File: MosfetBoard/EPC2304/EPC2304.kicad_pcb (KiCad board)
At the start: 4 copper layers, 120 x 75 mm, 170 parts, among them J10 DriverConn, J14 BATT-Conn2, J4 PhaseConn, J5 PhaseConn, J6 PhaseConn, J7 DriverConn, J8 DriverConn, J9 BATT-Conn1, Q1 EPC2304, Q13 EPC2304, Q14 EPC2304, Q15 EPC2304, Q2 EPC2304, Q3 EPC2304, Q4 EPC2304, Q5 EPC2304, Q6 EPC2304, Q7 EPC2304, Q8 EPC2304, Q9 EPC2304, U1 2EDF7275KXUMA1, U2 2EDF7275KXUMA1, U3 2EDF7275KXUMA1, U4 MT9223CT-50BR5, U5 MT9223CT-50BR5, U6 MT9223CT-50BR5

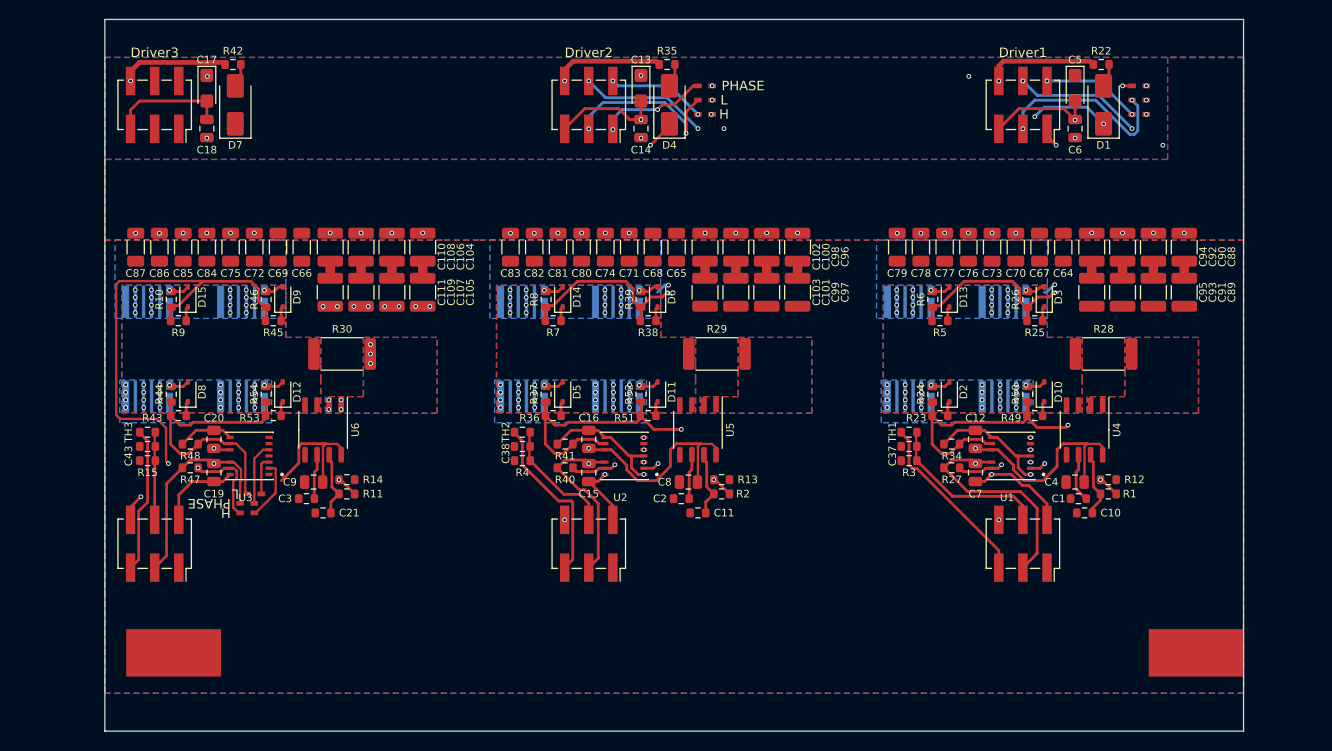
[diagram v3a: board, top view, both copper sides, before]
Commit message: v2.8.0 - Small Hall sensors
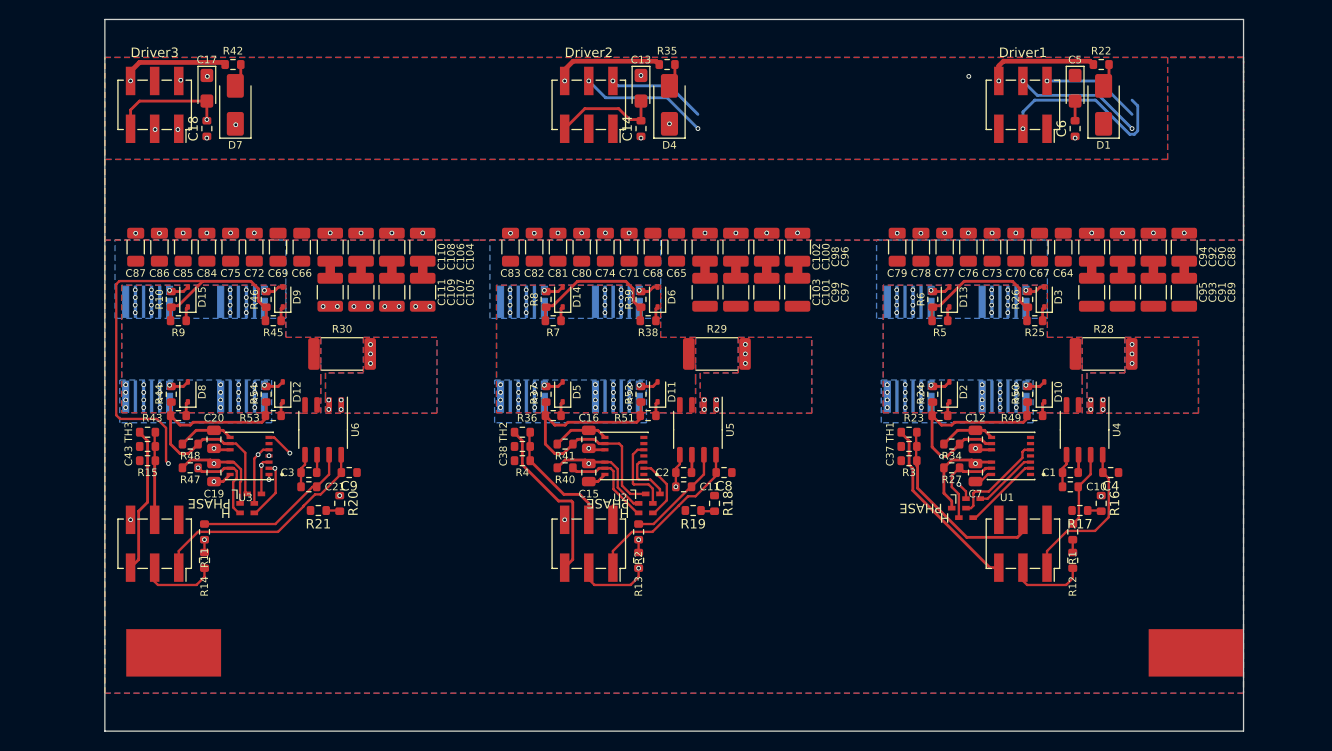
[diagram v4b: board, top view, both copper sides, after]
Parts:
- added R16: 150k, Resistor_SMD:R_0603_1608Metric, F.Cu at (210.0, 105.0)
- added R17: 2.7k, Resistor_SMD:R_0603_1608Metric, F.Cu at (207.8, 105.8)
- added R18: 150k, Resistor_SMD:R_0603_1608Metric, F.Cu at (169.2, 105.0)
- added R19: 2.7k, Resistor_SMD:R_0603_1608Metric, F.Cu at (167.0, 105.8)
- added R20: 150k, Resistor_SMD:R_0603_1608Metric, F.Cu at (129.8, 105.0)
- added R21: 2.7k, Resistor_SMD:R_0603_1608Metric, F.Cu at (127.5, 105.8)
- C14, C18, C4, C6, C8, C9: footprint Capacitor_SMD:C_0805_2012Metric -> GigaVescLibs:C_0603_1608Metric_L
- moved JP1 48.4 mm to (195.0, 105.5), turned to 180 degrees
- moved JP3 46.3 mm to (195.8, 106.5), turned to 180 degrees
- moved JP2 45.5 mm to (196.5, 104.5), turned to 180 degrees
- moved JP5 44.4 mm to (162.0, 105.0), turned to 180 degrees
- moved JP7 42.5 mm to (162.0, 106.0), turned to 180 degrees
- moved JP6 41.9 mm to (162.8, 104.0), turned to 180 degrees
- moved R14 17.2 mm to (115.5, 111.0), turned to 90 degrees
- moved R11 15.5 mm to (115.5, 108.0), turned to 90 degrees
- moved R13 12.2 mm to (161.2, 111.0), turned to 90 degrees
- moved R2 9.62 mm to (161.2, 108.0), turned to 90 degrees
- moved R12 9.29 mm to (207.0, 111.0), turned to 90 degrees
- moved R1 5.48 mm to (207.0, 108.0), turned to 90 degrees
- moved C4 3.88 mm to (211.0, 101.8), turned to 180 degrees
- moved C8 3.88 mm to (170.2, 101.8), turned to 180 degrees
- moved C9 3.88 mm to (130.8, 101.8), turned to 180 degrees
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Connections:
- net Net-(R28-Pad2) renamed /PhaseMosfets1/PHASE_OUT
- net Net-(R29-Pad2) renamed /PhaseMosfets2/PHASE_OUT
- net Net-(R30-Pad2) renamed /PhaseMosfets3/PHASE_OUT
- C1 pad 2: GNDA -> /PhaseMosfets1/SH-
- C10 pad 2: GNDA -> /PhaseMosfets1/SH-
- C11 pad 2: GNDA -> /PhaseMosfets2/SH-
- C15 pad 1: /PhaseMosfets2/FLOAT_VDD -> Net-(D4-K)
- C19 pad 1: /PhaseMosfets3/FLOAT_VDD -> Net-(D7-K)
- C2 pad 2: GNDA -> /PhaseMosfets2/SH-
- C21 pad 2: GNDA -> /PhaseMosfets3/SH-
- C3 pad 2: GNDA -> /PhaseMosfets3/SH-
- C4 pad 2: /PhaseMosfets1/DRV_POWER -> /PhaseMosfets1/5V_IN
- C7 pad 1: /PhaseMosfets1/FLOAT_VDD -> Net-(D1-K)
- C8 pad 2: /PhaseMosfets2/DRV_POWER -> /PhaseMosfets2/5V_IN
- C9 pad 2: /PhaseMosfets3/DRV_POWER -> /PhaseMosfets3/5V_IN
- D1 pad 1: /PhaseMosfets1/FLOAT_VDD -> Net-(D1-K)
- D4 pad 1: /PhaseMosfets2/FLOAT_VDD -> Net-(D4-K)
- D7 pad 1: /PhaseMosfets3/FLOAT_VDD -> Net-(D7-K)
- J4 pad 1: -BATT -> /PhaseMosfets1/5V_IN
- J4 pad 2: /PhaseMosfets1/FLOAT_VDD -> /PhaseMosfets1/V_SENSE
- J4 pad 3: GNDA -> /PhaseMosfets1/SH-
- J5 pad 1: -BATT -> /PhaseMosfets2/5V_IN
- J5 pad 2: /PhaseMosfets2/FLOAT_VDD -> /PhaseMosfets2/V_SENSE
- J5 pad 3: GNDA -> /PhaseMosfets2/SH-
- J6 pad 1: -BATT -> /PhaseMosfets3/5V_IN
- J6 pad 2: /PhaseMosfets3/FLOAT_VDD -> /PhaseMosfets3/V_SENSE
- J6 pad 3: GNDA -> /PhaseMosfets3/SH-
- R12 pad 1: GNDA -> /PhaseMosfets1/SH-
- R13 pad 1: GNDA -> /PhaseMosfets2/SH-
- R14 pad 1: GNDA -> /PhaseMosfets3/SH-
- U1 pad 13: /PhaseMosfets1/FLOAT_VDD -> Net-(D1-K)
- U2 pad 13: /PhaseMosfets2/FLOAT_VDD -> Net-(D4-K)
- U3 pad 13: /PhaseMosfets3/FLOAT_VDD -> Net-(D7-K)
- U4 pad 5: GNDA -> /PhaseMosfets1/SH-
- U4 pad 8: /PhaseMosfets1/DRV_POWER -> /PhaseMosfets1/5V_IN
- U5 pad 5: GNDA -> /PhaseMosfets2/SH-
- U5 pad 8: /PhaseMosfets2/DRV_POWER -> /PhaseMosfets2/5V_IN
- U6 pad 5: GNDA -> /PhaseMosfets3/SH-
- U6 pad 8: /PhaseMosfets3/DRV_POWER -> /PhaseMosfets3/5V_IN
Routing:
- net -BATT: track 143.0 -> 45.5 mm, vias 22 -> 20
- net Net-(D7-K): track 0.00 -> 81.6 mm, vias 0 -> 2
- net /PhaseMosfets3/H: track 6.38 -> 86.4 mm, vias 0 -> 2
- net /PhaseMosfets3/L: track 4.05 -> 82.2 mm, vias 0 -> 2
- net /PhaseMosfets3/LOCKOUT: track 6.66 -> 81.3 mm, vias 0 -> 2
- net /PhaseMosfets3/3.3V_IN: track 12.4 -> 86.1 mm, vias 0 -> 2
- net /PhaseMosfets1/FLOAT_VDD: track 59.1 -> 0.00 mm, vias 3 -> 0
- net /PhaseMosfets2/L: track 55.1 -> 5.63 mm, vias 3 -> 0
- net /PhaseMosfets1/PH: track 73.2 -> 25.3 mm, vias 3 -> 0
- net /PhaseMosfets2/FLOAT_VDD: track 47.0 -> 0.00 mm, vias 2 -> 0
- net /PhaseMosfets1/3.3V_IN: track 47.8 -> 1.95 mm, vias 2 -> 0
- net /PhaseMosfets2/PH: track 68.7 -> 26.0 mm, vias 3 -> 0
- net /PhaseMosfets1/PHASE: track 57.6 -> 16.4 mm, vias 43 -> 41
- net /PhaseMosfets2/LOCKOUT: track 48.4 -> 8.28 mm, vias 3 -> 0
- net /PhaseMosfets1/LOCKOUT: track 48.4 -> 10.5 mm, vias 3 -> 0
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
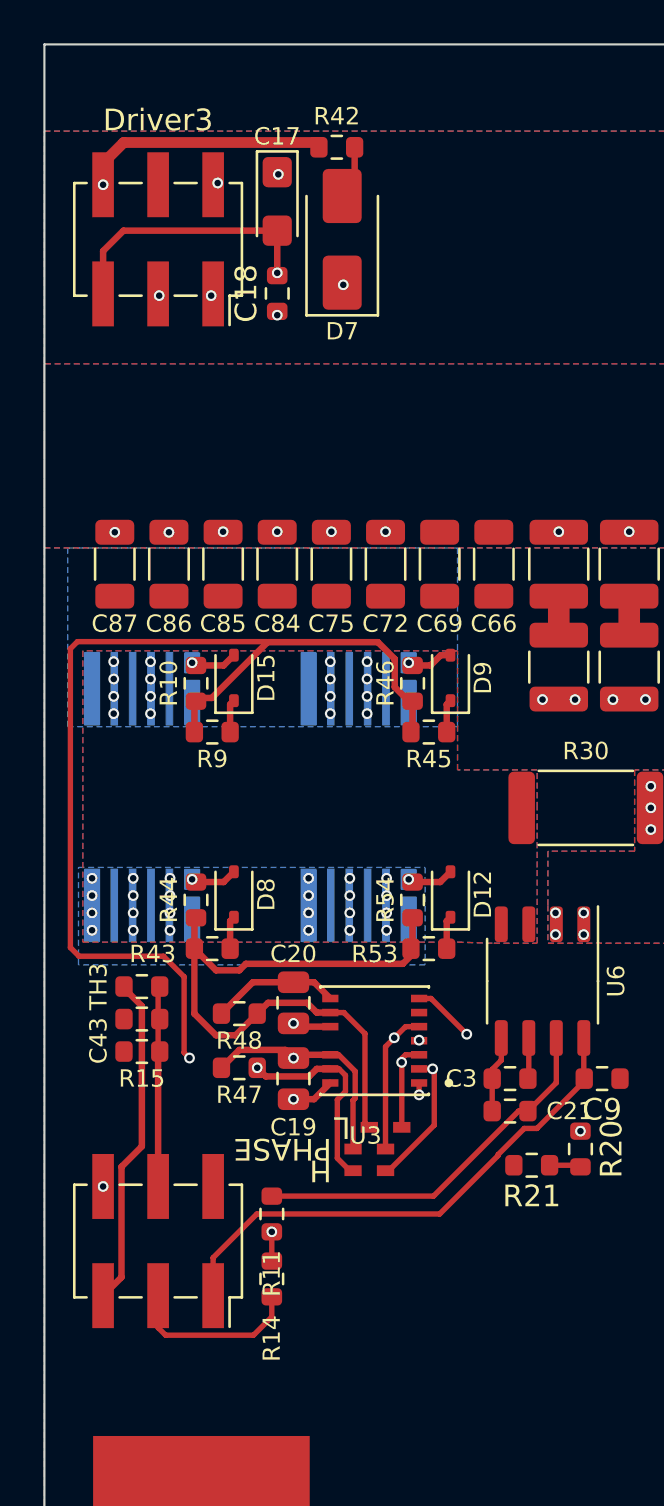
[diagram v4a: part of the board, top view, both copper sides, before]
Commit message: v2.10.0 - Low side shunt and hall sensor - logic routed
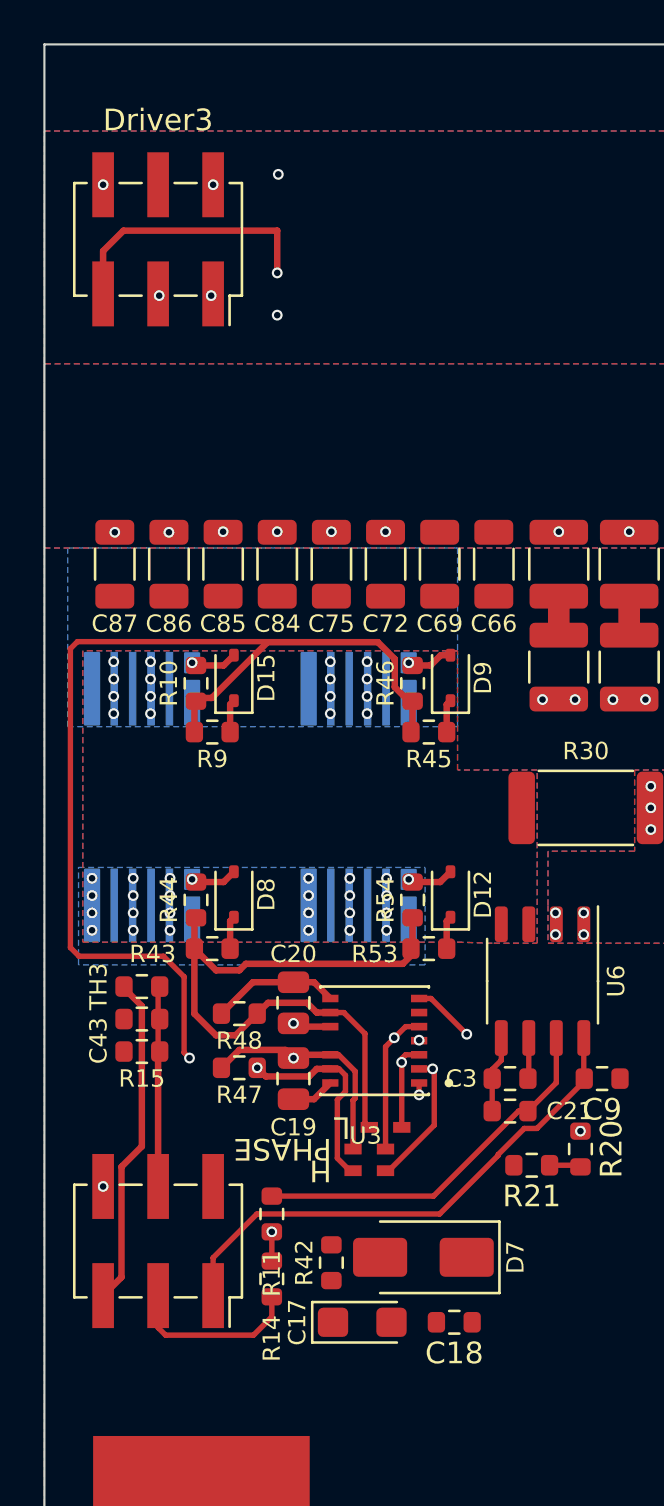
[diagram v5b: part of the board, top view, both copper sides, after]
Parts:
- moved C17 51.9 mm to (119.7, 113.0), turned to 0 degrees
- moved R42 51.5 mm to (118.2, 110.2), turned to -90 degrees
- moved C18 48.2 mm to (123.9, 113.0), turned to 180 degrees
- moved D7 47.1 mm to (122.5, 110.0), turned to 180 degrees
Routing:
- net Net-(D7-K): track 81.6 -> 2.01 mm, vias 2 -> 0
- net /PhaseMosfets3/DRV_POWER: track 61.1 -> 50.6 mm
- net Net-(D7-A): track 2.49 -> 0.00 mm

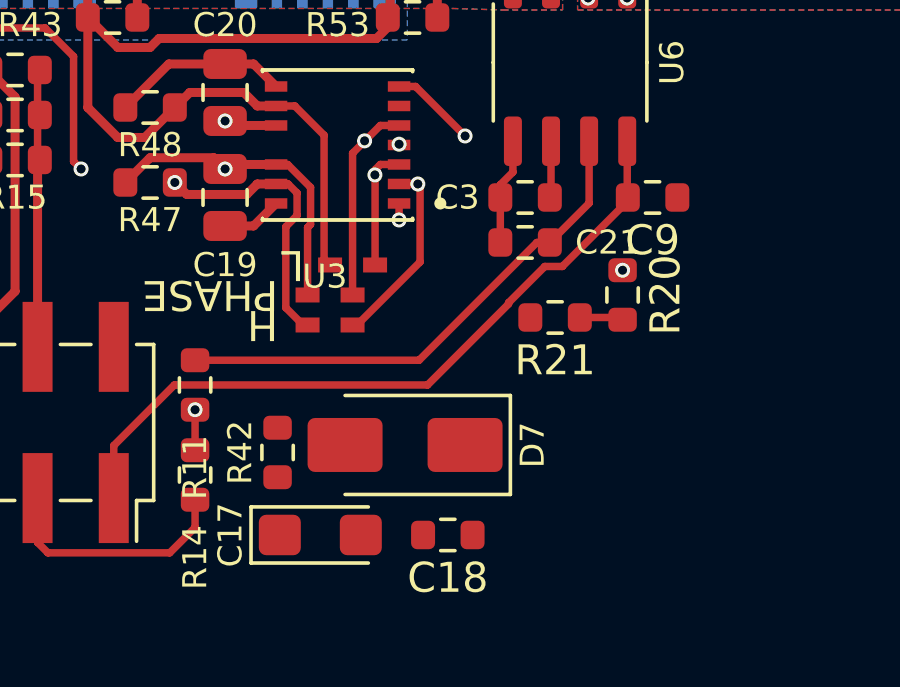
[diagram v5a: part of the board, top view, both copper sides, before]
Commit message: v2.10.0 - Low side shunt and hall sensor - current filters
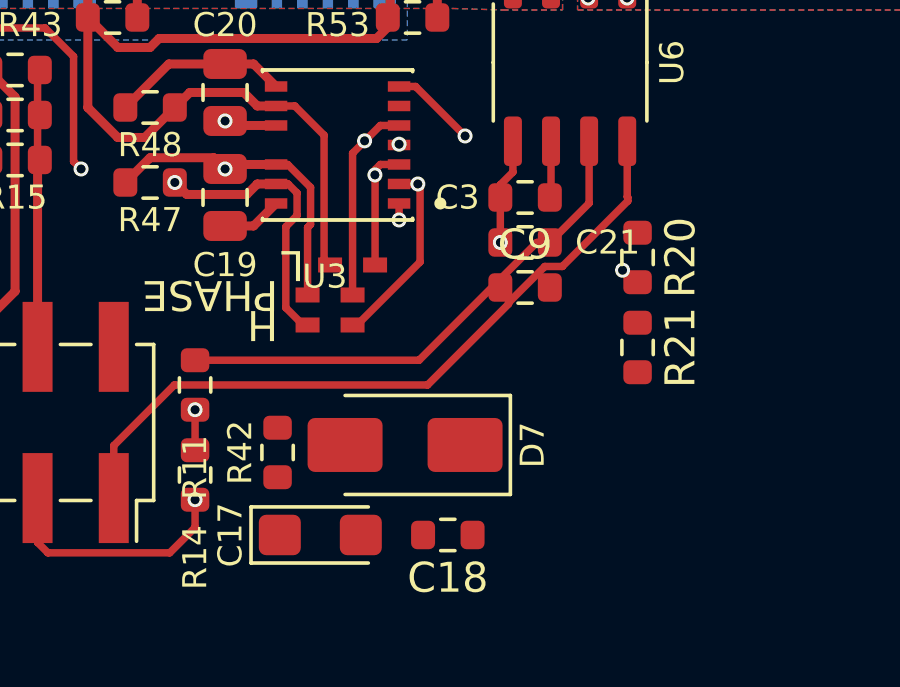
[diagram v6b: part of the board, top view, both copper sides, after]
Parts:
- moved C9 5.20 mm to (126.5, 104.8), turned to 0 degrees
- moved R21 2.93 mm to (130.2, 106.8), turned to -90 degrees
- moved R20 1.35 mm to (130.2, 103.8)
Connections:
- C4 pad 1: -BATT -> /PhaseMosfets1/SH-
- C8 pad 1: -BATT -> /PhaseMosfets2/SH-
- C9 pad 1: -BATT -> /PhaseMosfets3/SH-
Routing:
- net /PhaseMosfets3/SH-: track 11.7 -> 25.4 mm, vias 0 -> 2
- net /PhaseMosfets3/V_SENSE: track 1.46 -> 0.00 mm, vias 0 -> 1
- net /PhaseMosfets3/PHASE_OUT: vias 8 -> 7
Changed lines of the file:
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@@
       (stroke (width 0.1) (type solid)) (layer "F.Fab"))
     (pad "1" smd roundrect (at -0.825 0 180) (size 0.8 0.95) (layers "F.Cu" "F.Paste" "F.Mask") (roundrect_rratio 0.25)
-      (net 3 "-BATT") (pintype "passive"))
+      (net 11 "/PhaseMosfets1/SH-") (pintype "passive"))
     (pad "2" smd roundrect (at 0.825 0 180) (size 0.8 0.95) (layers "F.Cu" "F.Paste" "F.Mask") (roundrect_rratio 0.25)
       (net 78 "/PhaseMosfets1/5V_IN") (pintype "passive"))
@@
   )
   (footprint "Resistor_SMD:R_0603_1608Metric" (layer "F.Cu")
-    (at 127.5 105.75 180)
+    (at 130.25 106.75 -90)
     (descr "Resistor SMD 0603 (1608 Metric), square (rectangular) end terminal, IPC_7351 nominal, (Body size source: IPC-SM-782 page 72, https://www.pcb-3d.com/wordpress/wp-content/uploads/ipc-sm-782a_amendment_1_and_2.pdf), generated with kicad-footprint-generator")
     (tags "resistor")
@@
     (property "ki_keywords" "R res resistor")
     (attr smd)
-    (fp_text reference "R21" (at 0 -1.43) (layer "F.SilkS")
+    (fp_text reference "R21" (at 0 -1.43 -270) (layer "F.SilkS")
         (effects (font (size 1 1) (thickness 0.15)))
     )
-    (fp_text value "2.7k" (at 0 1.43) (layer "F.Fab")
+    (fp_text value "2.7k" (at 0 1.43 -270) (layer "F.Fab")
         (effects (font (size 1 1) (thickness 0.15)))
     )
-    (fp_text user "${REFERENCE}" (at 0 0) (layer "F.Fab")
+    (fp_text user "${REFERENCE}" (at 0 0 -270) (layer "F.Fab")
         (effects (font (size 0.4 0.4) (thickness 0.06)))
     )
@@
     (fp_line (start 0.8 0.4125) (end -0.8 0.4125)
       (stroke (width 0.1) (type solid)) (layer "F.Fab"))
-    (pad "1" smd roundrect (at -0.825 0 180) (size 0.8 0.95) (layers "F.Cu" "F.Paste" "F.Mask") (roundrect_rratio 0.25)
+    (pad "1" smd roundrect (at -0.825 0 270) (size 0.8 0.95) (layers "F.Cu" "F.Paste" "F.Mask") (roundrect_rratio 0.25)
       (net 95 "/PhaseMosfets3/V_SENSE") (pintype "passive"))
-    (pad "2" smd roundrect (at 0.825 0 180) (size 0.8 0.95) (layers "F.Cu" "F.Paste" "F.Mask") (roundrect_rratio 0.25)
+    (pad "2" smd roundrect (at 0.825 0 270) (size 0.8 0.95) (layers "F.Cu" "F.Paste" "F.Mask") (roundrect_rratio 0.25)
       (net 3 "-BATT") (pintype "passive"))
     (model "${KICAD6_3DMODEL_DIR}/Resistor_SMD.3dshapes/R_0603_1608Metric.wrl"
@@
       (stroke (width 0.1) (type solid)) (layer "F.Fab"))
     (pad "1" smd roundrect (at -0.825 0 180) (size 0.8 0.95) (layers "F.Cu" "F.Paste" "F.Mask") (roundrect_rratio 0.25)
-      (net 3 "-BATT") (pintype "passive"))
+      (net 17 "/PhaseMosfets2/SH-") (pintype "passive"))
     (pad "2" smd roundrect (at 0.825 0 180) (size 0.8 0.95) (layers "F.Cu" "F.Paste" "F.Mask") (roundrect_rratio 0.25)
       (net 80 "/PhaseMosfets2/5V_IN") (pintype "passive"))
@@
   )
   (footprint "Resistor_SMD:R_0603_1608Metric" (layer "F.Cu")
-    (at 129.75 105 -90)
+    (at 130.25 103.75 -90)
     (descr "Resistor SMD 0603 (1608 Metric), square (rectangular) end terminal, IPC_7351 nominal, (Body size source: IPC-SM-782 page 72, https://www.pcb-3d.com/wordpress/wp-content/uploads/ipc-sm-782a_amendment_1_and_2.pdf), generated with kicad-footprint-generator")
     (tags "resistor")
@@
   )
   (footprint "GigaVescLibs:C_0603_1608Metric_L" (layer "F.Cu")
-    (at 130.75 101.75 180)
+    (at 126.5 104.75)
     (descr "Resistor SMD 0603 (1608 Metric), square (rectangular) end terminal, IPC_7351 nominal, (Body size source: IPC-SM-782 page 72, https://www.pcb-3d.com/wordpress/wp-content/uploads/ipc-sm-782a_amendment_1_and_2.pdf), generated with kicad-footprint-generator")
     (tags "resistor")
@@
     (fp_line (start 0.8 0.4125) (end -0.8 0.4125)
       (stroke (width 0.1) (type solid)) (layer "F.Fab"))
-    (pad "1" smd roundrect (at -0.825 0 180) (size 0.8 0.95) (layers "F.Cu" "F.Paste" "F.Mask") (roundrect_rratio 0.25)
-      (net 3 "-BATT") (pintype "passive"))
-    (pad "2" smd roundrect (at 0.825 0 180) (size 0.8 0.95) (layers "F.Cu" "F.Paste" "F.Mask") (roundrect_rratio 0.25)
+    (pad "1" smd roundrect (at -0.825 0) (size 0.8 0.95) (layers "F.Cu" "F.Paste" "F.Mask") (roundrect_rratio 0.25)
+      (net 23 "/PhaseMosfets3/SH-") (pintype "passive"))
+    (pad "2" smd roundrect (at 0.825 0) (size 0.8 0.95) (layers "F.Cu" "F.Paste" "F.Mask") (roundrect_rratio 0.25)
       (net 90 "/PhaseMosfets3/5V_IN") (pintype "passive"))
     (model "${KICAD7_3DMODEL_DIR}/Capacitor_SMD.3dshapes/C_0603_1608Metric.wrl"
@@
   (segment (start 125.675 101.325) (end 125.675 101.75) (width 0.25) (layer "F.Cu") (net 23))
   (segment (start 115.5 112.75) (end 114.655 113.595) (width 0.25) (layer "F.Cu") (net 23))
+  (via (at 115.5 111.825) (size 0.5) (drill 0.3) (layers "F.Cu" "B.Cu") (net 23))
+  (via (at 125.675 103.25) (size 0.5) (drill 0.3) (layers "F.Cu" "B.Cu") (net 23))
+  (segment (start 124.075 103.25) (end 125.675 103.25) (width 0.25) (layer "In2.Cu") (net 23))
+  (segment (start 115.5 111.825) (end 124.075 103.25) (width 0.25) (layer "In2.Cu") (net 23))
   (segment (start 210.825 60.425) (end 210.25 61) (width 0.3) (layer "F.Cu") (net 24))
   (segment (start 210.825 58.75) (end 210.825 60.425) (width 0.3) (layer "F.Cu") (net 24))
@@
   (segment (start 167.9 105.825) (end 167.825 105.75) (width 0.25) (layer "F.Cu") (net 94))
   (segment (start 169.25 105.825) (end 167.9 105.825) (width 0.25) (layer "F.Cu") (net 94))
-  (segment (start 129.675 105.75) (end 129.75 105.825) (width 0.25) (layer "F.Cu") (net 95))
-  (segment (start 128.325 105.75) (end 129.675 105.75) (width 0.25) (layer "F.Cu") (net 95))
+  (via (at 129.75 104.175) (size 0.5) (drill 0.3) (layers "F.Cu" "B.Cu") (net 95))
   (segment (start 210 104.175) (end 210 104.25) (width 0.25) (layer "F.Cu") (net 96))
   (via (at 210.2 95.1) (size 0.5) (drill 0.3) (layers "F.Cu" "B.Cu") (net 96))
@@
   (via (at 129.9 95.1) (size 0.5) (drill 0.3) (layers "F.Cu" "B.Cu") (net 98))
   (via (at 128.6 95.1) (size 0.5) (drill 0.3) (layers "F.Cu" "B.Cu") (net 98))
-  (via (at 129.75 104.175) (size 0.5) (drill 0.3) (layers "F.Cu" "B.Cu") (net 98))
   (segment (start 129.75 95.25) (end 129.9 95.1) (width 0.25) (layer "In2.Cu") (net 98))
   (zone (net 0) (net_name "") (layer "F.Cu") (name "Cleanup") (hatch edge 0.5)
